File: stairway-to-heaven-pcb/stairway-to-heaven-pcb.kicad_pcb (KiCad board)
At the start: 2 copper layers, 99.8 x 97.3 mm, 113 parts, among them J1 Conn_01x04_Male, J10 Conn_01x04_Male, J11 Conn_01x04_Male, J12 Conn_01x04_Male, J13 Conn_01x04_Male, J14 Conn_01x04_Male, J15 PJ-063AH, J2 Conn_01x04_Male, J3 Conn_01x04_Male, J4 Conn_01x04_Male, J5 Conn_01x04_Male, J6 Conn_01x04_Male, J7 Conn_01x04_Male, J8 Conn_01x04_Male, J9 Conn_01x04_Male, Q1 FDN337N, Q10 FDN337N, Q11 FDN337N, Q12 FDN337N, Q13 FDN337N, Q14 FDN337N, Q15 FDN337N, Q16 FDN337N, Q17 FDN337N, Q18 FDN337N, Q19 FDN337N, Q2 FDN337N, Q20 FDN337N, Q21 FDN337N, Q22 FDN337N, Q23 FDN337N, Q24 FDN337N, Q25 FDN337N, Q26 FDN337N, Q27 FDN337N, Q28 FDN337N, Q29 FDN337N, Q3 FDN337N, Q30 FDN337N, Q31 FDN337N, Q32 FDN337N, Q33 FDN337N, Q34 FDN337N, Q35 FDN337N, Q36 FDN337N, Q37 FDN337N, Q38 FDN337N, Q39 FDN337N, Q4 FDN337N, Q40 FDN337N, Q41 FDN337N, Q42 FDN337N, Q5 FDN337N, Q6 FDN337N, Q7 FDN337N, Q8 FDN337N, Q9 FDN337N, U1 MEGA_PRO_EMBED_CH340G_{slash}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, U2 LM2575T-5.0

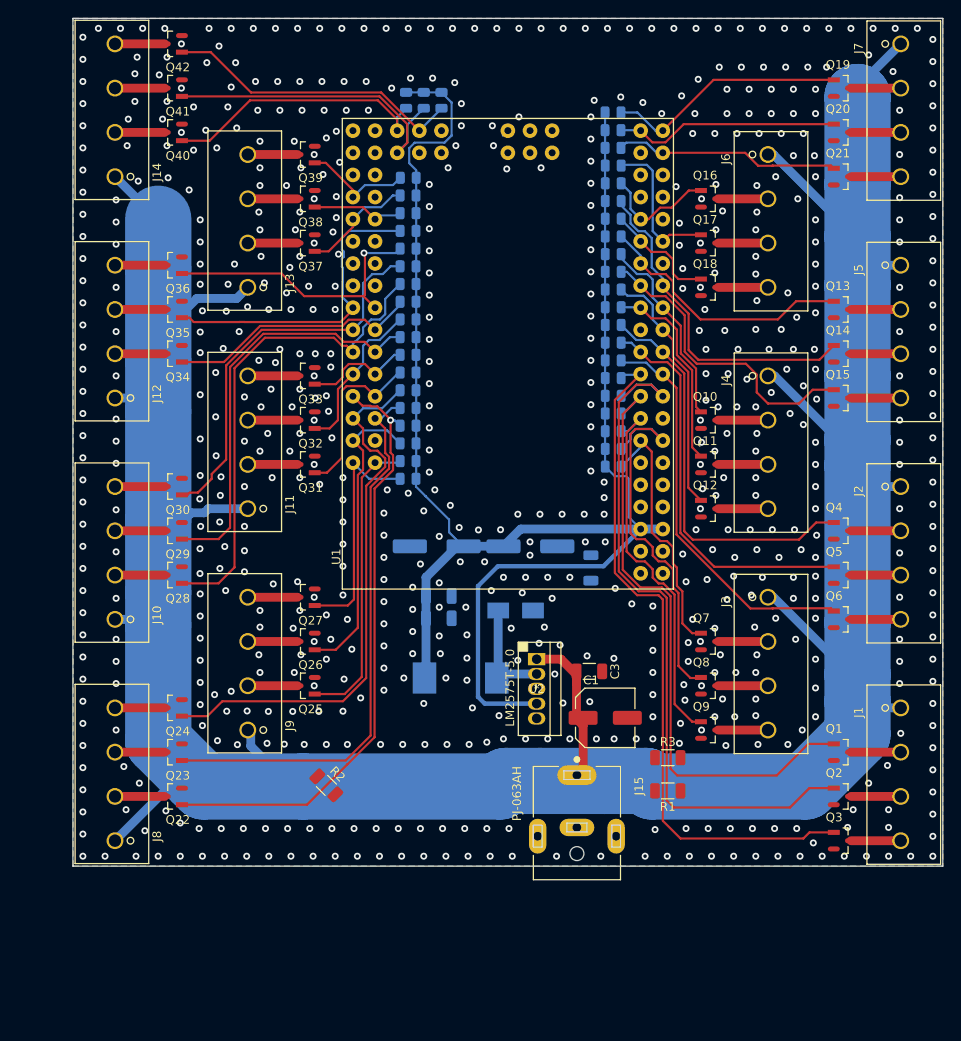
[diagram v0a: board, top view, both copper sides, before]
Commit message: Change to 4 layer pcb. Routing leds done.
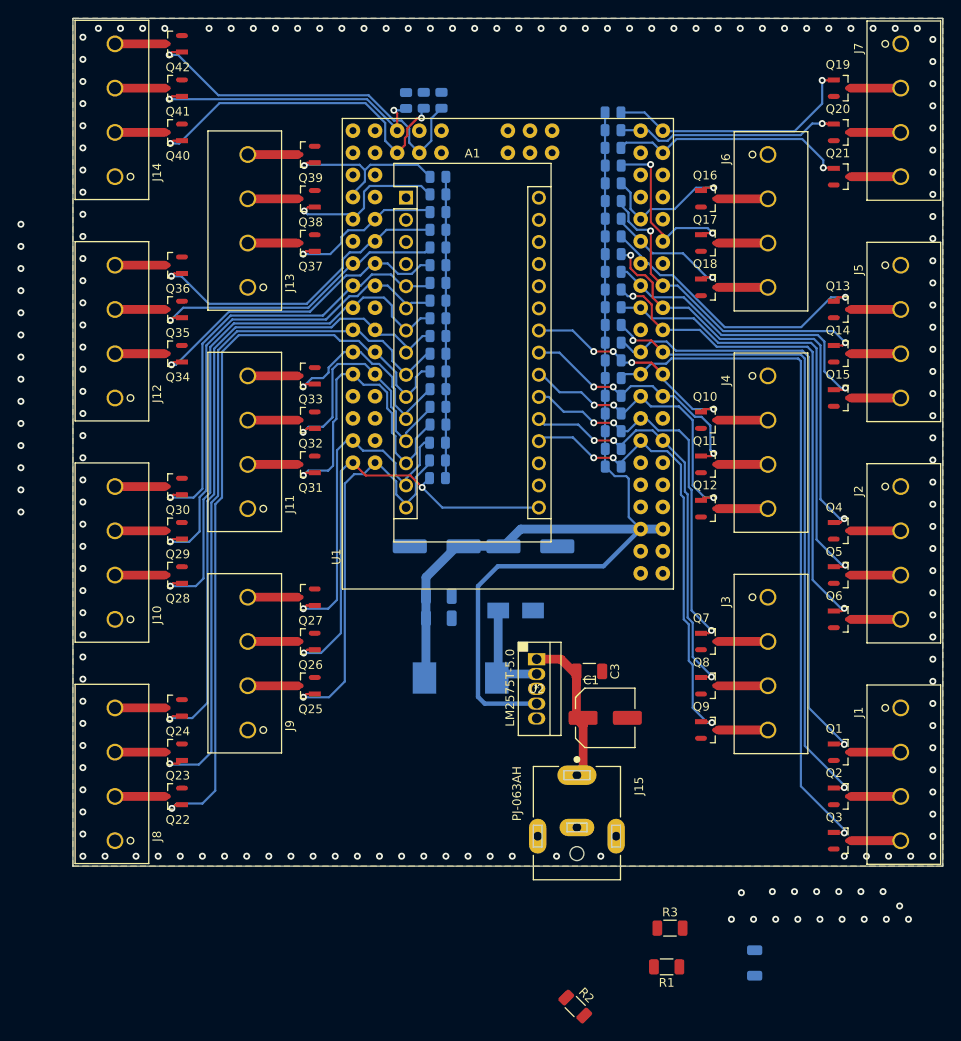
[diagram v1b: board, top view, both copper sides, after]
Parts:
- added A1: Arduino_Nano_v2.x, Module:Arduino_Nano, F.Cu at (139.4, 62.1)
- moved R46 49.1 mm to (179.5, 149.9)
- moved R2 38.2 mm to (158.9, 154.9)
- moved R1 20.2 mm to (169.4, 150.4)
- moved R3 19.6 mm to (169.7, 145.9)
- moved R15 14.2 mm to (163.2, 86.9)
- moved R13 12.2 mm to (163.2, 80.8)
- moved R35 10.6 mm to (143.1, 86.1)
- moved R14 10.2 mm to (163.2, 84.8)
- moved R4 8.13 mm to (163.2, 78.7)
- moved R5 8.13 mm to (163.2, 76.7)
- moved R7 8.13 mm to (163.2, 68.6)
- moved R9 8.13 mm to (163.2, 72.6)
- moved R25 7.11 mm to (143.1, 82.0)
- moved R26 7.11 mm to (143.1, 80.0)
- moved R27 7.11 mm to (143.1, 78.0)
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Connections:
- net /Fets1/B_EN renamed /LED1B_EN
- net /Fets13/B_EN renamed /LED13B_EN
- net /Fets5/B_EN renamed /LED5B_EN
- net /Fets5/G_EN renamed /LED5G_EN
- net /Fets6/B_EN renamed /LED6B_EN
- net /Fets6/G_EN renamed /LED6G_EN
- net /Fets7/B_EN renamed /LED7B_EN
- net /Fets7/G_EN renamed /LED7G_EN
- Q1 pad 1: /Fets1/G_EN -> /LED1G_EN
- Q10 pad 1: /Fets4/G_EN -> /LED4G_EN
- Q12 pad 1: /Fets4/B_EN -> /LED4B_EN
- Q22 pad 1: /Fets8/G_EN -> /LED8G_EN
- Q24 pad 1: /Fets8/B_EN -> /LED8B_EN
- Q26 pad 1: /Fets9/R_EN -> /LED9R_EN
- Q27 pad 1: /Fets9/B_EN -> /LED9B_EN
- Q28 pad 1: /Fets10/G_EN -> /LED10G_EN
- Q30 pad 1: /Fets10/B_EN -> /LED10B_EN
- Q31 pad 1: /Fets11/G_EN -> /LED11G_EN
- Q33 pad 1: /Fets11/B_EN -> /LED11B_EN
- Q34 pad 1: /Fets12/G_EN -> /LED12G_EN
- Q36 pad 1: /Fets12/B_EN -> /LED12B_EN
- Q37 pad 1: /Fets13/G_EN -> /LED13G_EN
- Q4 pad 1: /Fets3/G_EN -> /LED3G_EN
- Q40 pad 1: /Fets14/G_EN -> /LED14G_EN
- Q42 pad 1: /Fets14/B_EN -> /LED14B_EN
- Q6 pad 1: /Fets3/B_EN -> /LED3B_EN
- Q7 pad 1: /Fets2/G_EN -> /LED2G_EN
- Q9 pad 1: /Fets2/B_EN -> /LED2B_EN
- R10 pad 2: /Fets2/G_EN -> /LED2G_EN
- R12 pad 2: /Fets2/B_EN -> /LED2B_EN
- R13 pad 2: /Fets4/G_EN -> /LED4G_EN
- R15 pad 2: /Fets4/B_EN -> /LED4B_EN
- R25 pad 2: /Fets8/G_EN -> /LED8G_EN
- R27 pad 2: /Fets8/B_EN -> /LED8B_EN
- R29 pad 2: /Fets9/R_EN -> /LED9R_EN
- R30 pad 2: /Fets9/B_EN -> /LED9B_EN
- R31 pad 2: /Fets10/G_EN -> /LED10G_EN
- R33 pad 2: /Fets10/B_EN -> /LED10B_EN
- R34 pad 2: /Fets11/G_EN -> /LED11G_EN
- R36 pad 2: /Fets11/B_EN -> /LED11B_EN
- R37 pad 2: /Fets12/G_EN -> /LED12G_EN
- R39 pad 2: /Fets12/B_EN -> /LED12B_EN
- R4 pad 2: /Fets1/G_EN -> /LED1G_EN
- R40 pad 2: /Fets13/G_EN -> /LED13G_EN
- R43 pad 2: /Fets14/G_EN -> /LED14G_EN
- R45 pad 2: /Fets14/B_EN -> /LED14B_EN
- R7 pad 2: /Fets3/G_EN -> /LED3G_EN
- R9 pad 2: /Fets3/B_EN -> /LED3B_EN
- U1 pad A0: /Fets9/B_EN -> /LED9R_EN
- U1 pad A10: /Fets10/G_EN -> /LED11B_EN
- U1 pad A11: /LED10R_EN -> /LED8G_EN
- U1 pad A12: /Fets10/B_EN -> /LED8R_EN
- U1 pad A13: /Fets12/G_EN -> /LED8B_EN
- U1 pad A14: /LED12R_EN -> /LED10G_EN
- U1 pad A15: /Fets12/B_EN -> unconnected-(U1-PadA15)
- U1 pad A2: /Fets9/R_EN -> /LED9B_EN
- U1 pad A4: /Fets8/B_EN -> unconnected-(U1-PadA4)
- U1 pad A5: /LED8R_EN -> unconnected-(U1-PadA5)
- U1 pad A6: /Fets8/G_EN -> unconnected-(U1-PadA6)
- U1 pad A7: /Fets11/G_EN -> unconnected-(U1-PadA7)
- U1 pad A8: /LED11R_EN -> /LED11G_EN
- U1 pad A9: /Fets11/B_EN -> /LED11R_EN
- U1 pad D10: /LED3R_EN -> /LED1G_EN
- U1 pad D11: /Fets3/G_EN -> /LED1R_EN
- U1 pad D13: /Fets4/B_EN -> /LED3B_EN
- U1 pad D14: /LED4R_EN -> /LED3R_EN
- U1 pad D15: /Fets4/G_EN -> /LED3G_EN
- U1 pad D2: /Fets2/G_EN -> /LED2B_EN
- U1 pad D32: unconnected-(U1-PadD32) -> /LED10B_EN
- U1 pad D33: unconnected-(U1-PadD33) -> /LED10R_EN
- U1 pad D34: unconnected-(U1-PadD34) -> /LED12R_EN
- U1 pad D35: unconnected-(U1-PadD35) -> /LED12G_EN
- U1 pad D37: unconnected-(U1-PadD37) -> /LED12B_EN
- U1 pad D38: /Fets13/G_EN -> /LED13R_EN
- U1 pad D39: /LED13R_EN -> /LED13G_EN
- U1 pad D4: /Fets2/B_EN -> /LED2G_EN
- U1 pad D48: /Fets14/G_EN -> /LED14R_EN
- U1 pad D49: /LED14R_EN -> /LED14G_EN
- U1 pad D50: /Fets14/B_EN -> unconnected-(U1-PadD50)
- U1 pad D51: unconnected-(U1-PadD51) -> /LED14B_EN
- U1 pad D6: /Fets1/G_EN -> /LED4B_EN
- U1 pad D7: /LED1R_EN -> /LED4R_EN
- U1 pad D9: /Fets3/B_EN -> /LED4G_EN
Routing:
- net +12V: track 374.7 -> 17.0 mm
- net /LED8G_EN: track 0.00 -> 88.3 mm, vias 0 -> 1
- net /LED8B_EN: track 0.00 -> 76.7 mm, vias 0 -> 1
- net /Fets1/G_EN: track 70.9 -> 0.00 mm
- net /LED1G_EN: track 0.00 -> 70.6 mm, vias 0 -> 1
- net /Fets8/G_EN: track 69.5 -> 0.00 mm, vias 1 -> 0
- net /LED10G_EN: track 0.00 -> 63.0 mm, vias 0 -> 1
- net /Fets8/B_EN: track 62.4 -> 0.00 mm
- net /LED3B_EN: track 0.00 -> 58.4 mm, vias 0 -> 2
- net /Fets10/G_EN: track 56.0 -> 0.00 mm
- net /LED2B_EN: track 0.00 -> 53.5 mm, vias 0 -> 3
- net /LED10B_EN: track 0.00 -> 52.3 mm, vias 0 -> 1
- net /LED9R_EN: track 0.00 -> 51.9 mm, vias 0 -> 2
- net /LED3G_EN: track 0.00 -> 51.8 mm, vias 0 -> 2
- net /Fets3/B_EN: track 46.2 -> 0.00 mm
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- added copper zone on In2.Cu, net +12V
- added copper zone on In1.Cu, net GND
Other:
- copper layers 2 -> 4

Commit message: minor tweaks to routing
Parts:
- removed R1, R2, R3, R46: 0R, Resistor_SMD:R_1206_3216Metric
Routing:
- net /LED14R_EN: track 33.3 -> 32.5 mm
- net GND: vias 169 -> 164

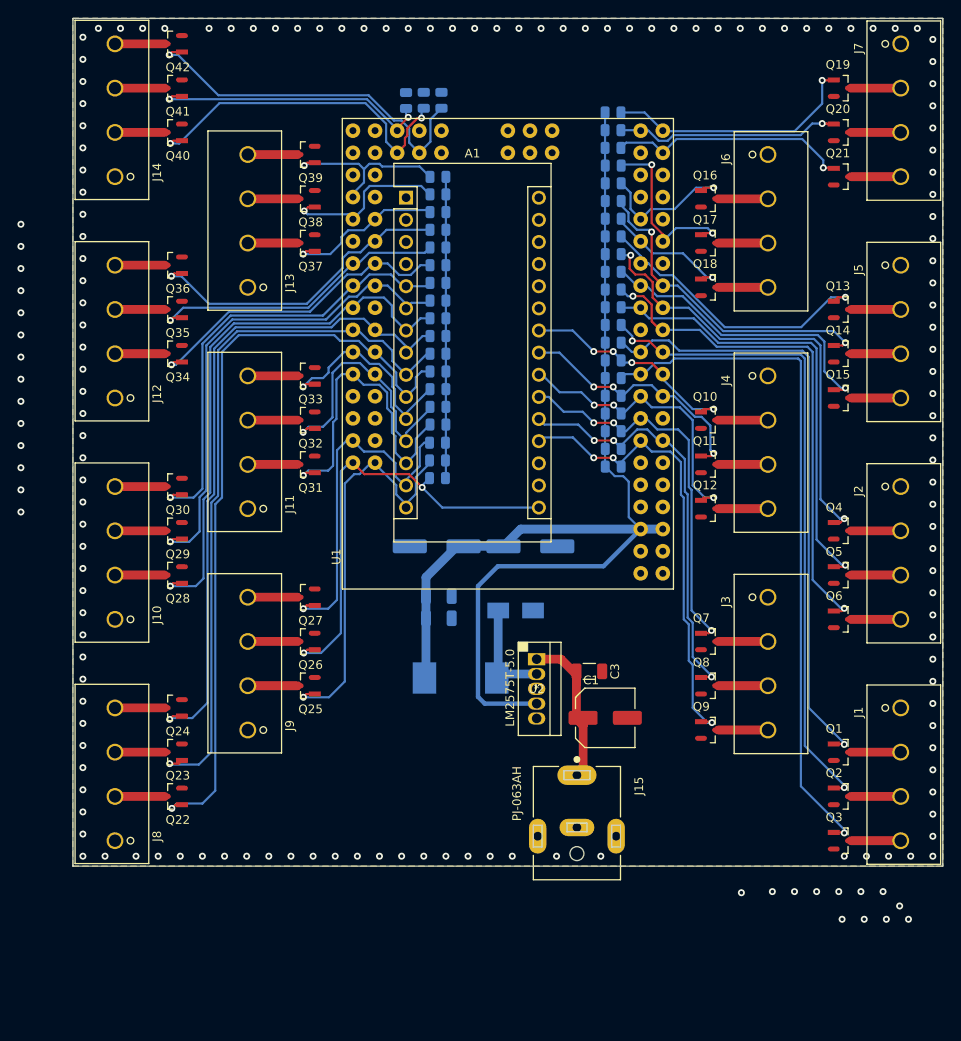
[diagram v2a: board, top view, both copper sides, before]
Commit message: PSU, again.. Stitching. Moved arduino nano.
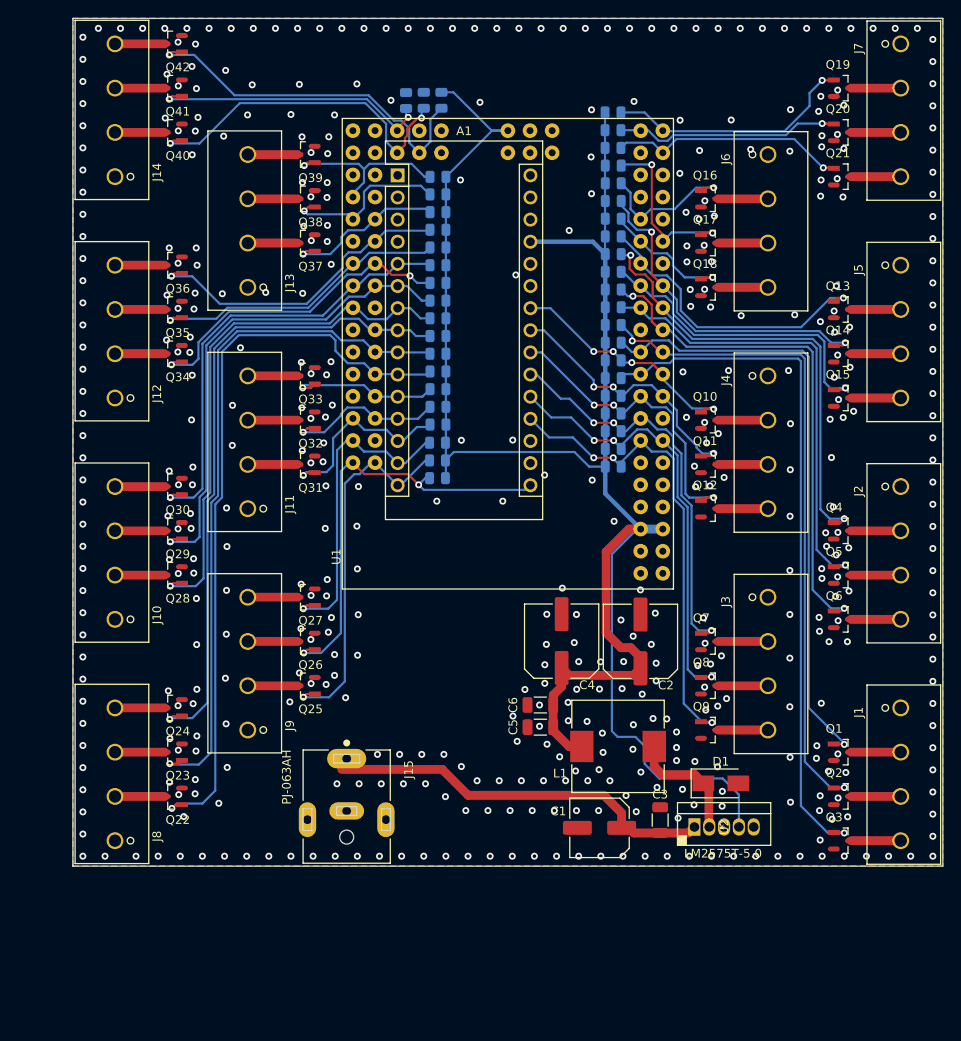
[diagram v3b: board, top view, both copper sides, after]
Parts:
- C2, C4, C5, C6, D1, L1: moved to F.Cu
- moved D1 30.8 mm to (175.6, 129.3)
- moved U2 26.7 mm to (175.9, 134.3), turned to 90 degrees
- moved J15 26.5 mm to (132.6, 126.5)
- moved C2 25.8 mm to (166.3, 113.0), turned to 90 degrees
- moved L1 19.7 mm to (163.8, 125.1)
- moved C3 18.9 mm to (168.6, 133.5), turned to -90 degrees
- moved C5 17.1 mm to (154.9, 122.9), turned to 180 degrees
- moved C6 17.1 mm to (154.9, 120.3), turned to 180 degrees
- moved C1 12.6 mm to (161.6, 134.4), turned to 180 degrees
- moved C4 11.5 mm to (157.3, 113.0), turned to 90 degrees
- moved A1 2.74 mm to (138.5, 59.5)
- moved R33 2.03 mm to (143.1, 69.8)
- moved R37 2.03 mm to (143.1, 71.9)
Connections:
- U1 pad A10: /LED11B_EN -> unconnected-(U1-PadA10)
- U1 pad A11: /LED8G_EN -> /LED8R_EN
- U1 pad A12: /LED8R_EN -> unconnected-(U1-PadA12)
- U1 pad A4: unconnected-(U1-PadA4) -> /LED11G_EN
- U1 pad A5: unconnected-(U1-PadA5) -> /LED11R_EN
- U1 pad A7: unconnected-(U1-PadA7) -> /LED11B_EN
- U1 pad A8: /LED11G_EN -> unconnected-(U1-PadA8)
- U1 pad A9: /LED11R_EN -> /LED8G_EN
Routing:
- net +5V: track 165.7 -> 223.3 mm
- net +12V: track 17.0 -> 44.8 mm
- net /LED11G_EN: track 36.9 -> 22.4 mm
- net /LED11R_EN: track 30.8 -> 18.5 mm
- net /LED11B_EN: track 24.9 -> 17.2 mm
- net /LED9B_EN: track 40.7 -> 36.0 mm
- net /LED9G_EN: track 47.3 -> 42.6 mm
- net /LED8G_EN: track 88.3 -> 85.2 mm
- net /LED2R_EN: track 48.3 -> 51.2 mm
- net /LED8R_EN: track 82.5 -> 79.7 mm
- net /LED4B_EN: track 33.6 -> 35.7 mm
- net /LED2G_EN: track 44.9 -> 46.9 mm
- net /LED4R_EN: track 29.2 -> 31.2 mm
- net /LED4G_EN: track 25.8 -> 27.8 mm
- net /LED8B_EN: track 76.7 -> 74.7 mm
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
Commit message: Add CA6V potentiometer footprint. Mounting holes.
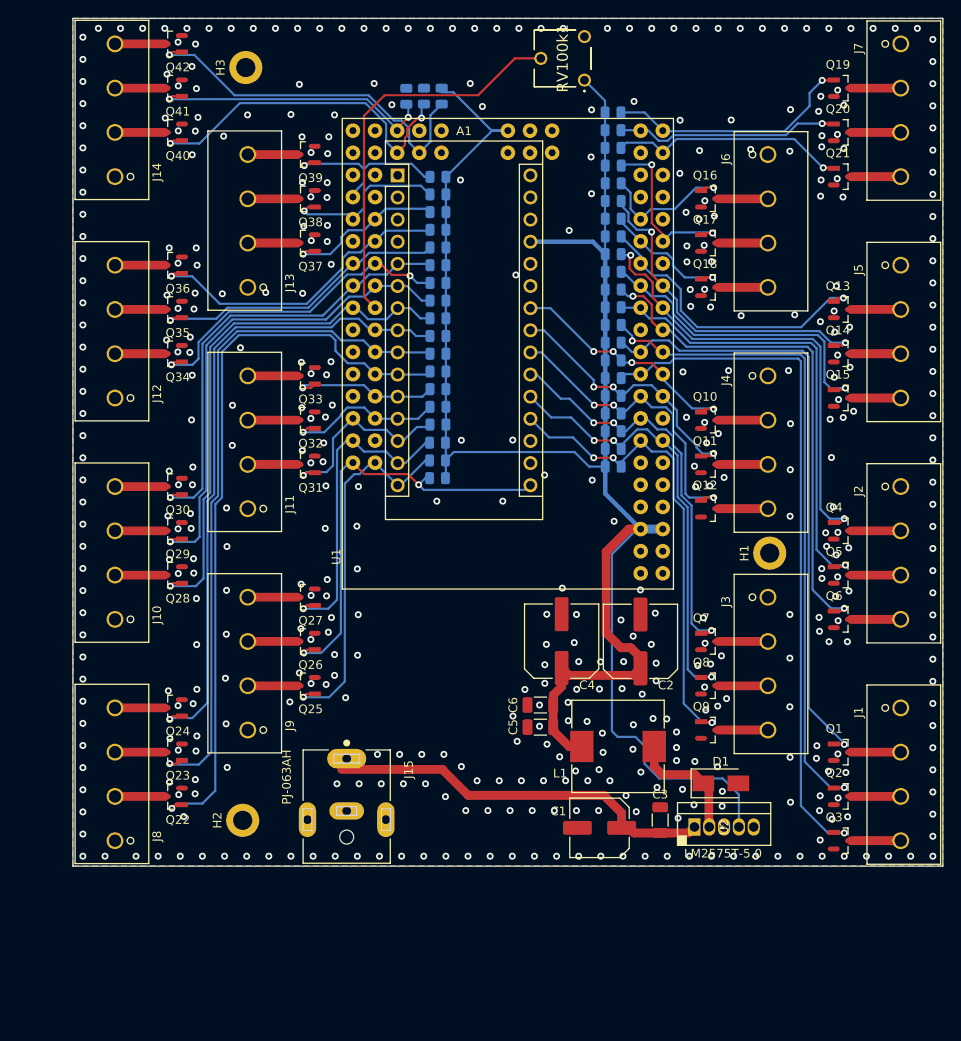
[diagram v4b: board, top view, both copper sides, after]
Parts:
- added H1: MountingHole_Pad, MountingHole:MountingHole_2.2mm_M2_DIN965_Pad, F.Cu at (181.2, 102.9)
- added H2: MountingHole_Pad, MountingHole:MountingHole_2.2mm_M2_DIN965_Pad, F.Cu at (120.7, 133.6)
- added H3: MountingHole_Pad, MountingHole:MountingHole_2.2mm_M2_DIN965_Pad, F.Cu at (121.1, 47.2)
- added RV100k1: R_Potentiometer_Trim, CA6V Potentiometer THT:CA6V-NoMidHole, F.Cu at (159.9, 48.6)
- moved R45 0.48 mm to (143.5, 50.4)
- moved R43 0.48 mm to (141.5, 50.4)
- moved R44 0.48 mm to (139.5, 50.5)
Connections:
- U1 pad A15: unconnected-(U1-PadA15) -> /POT1
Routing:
- net /POT1: track 0.00 -> 45.6 mm
- net +5V: track 223.3 -> 228.0 mm
- net GND: vias 469 -> 464
